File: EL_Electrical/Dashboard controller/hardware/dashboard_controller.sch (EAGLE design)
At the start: 48 parts, among them IC1 MCP2562-E_SN, IC2 MCP2515-I_SO, J1 22-05-7098-09, Q1 BSS138, Q2 BSS138, Q3 BSS138, Q6 BSS138

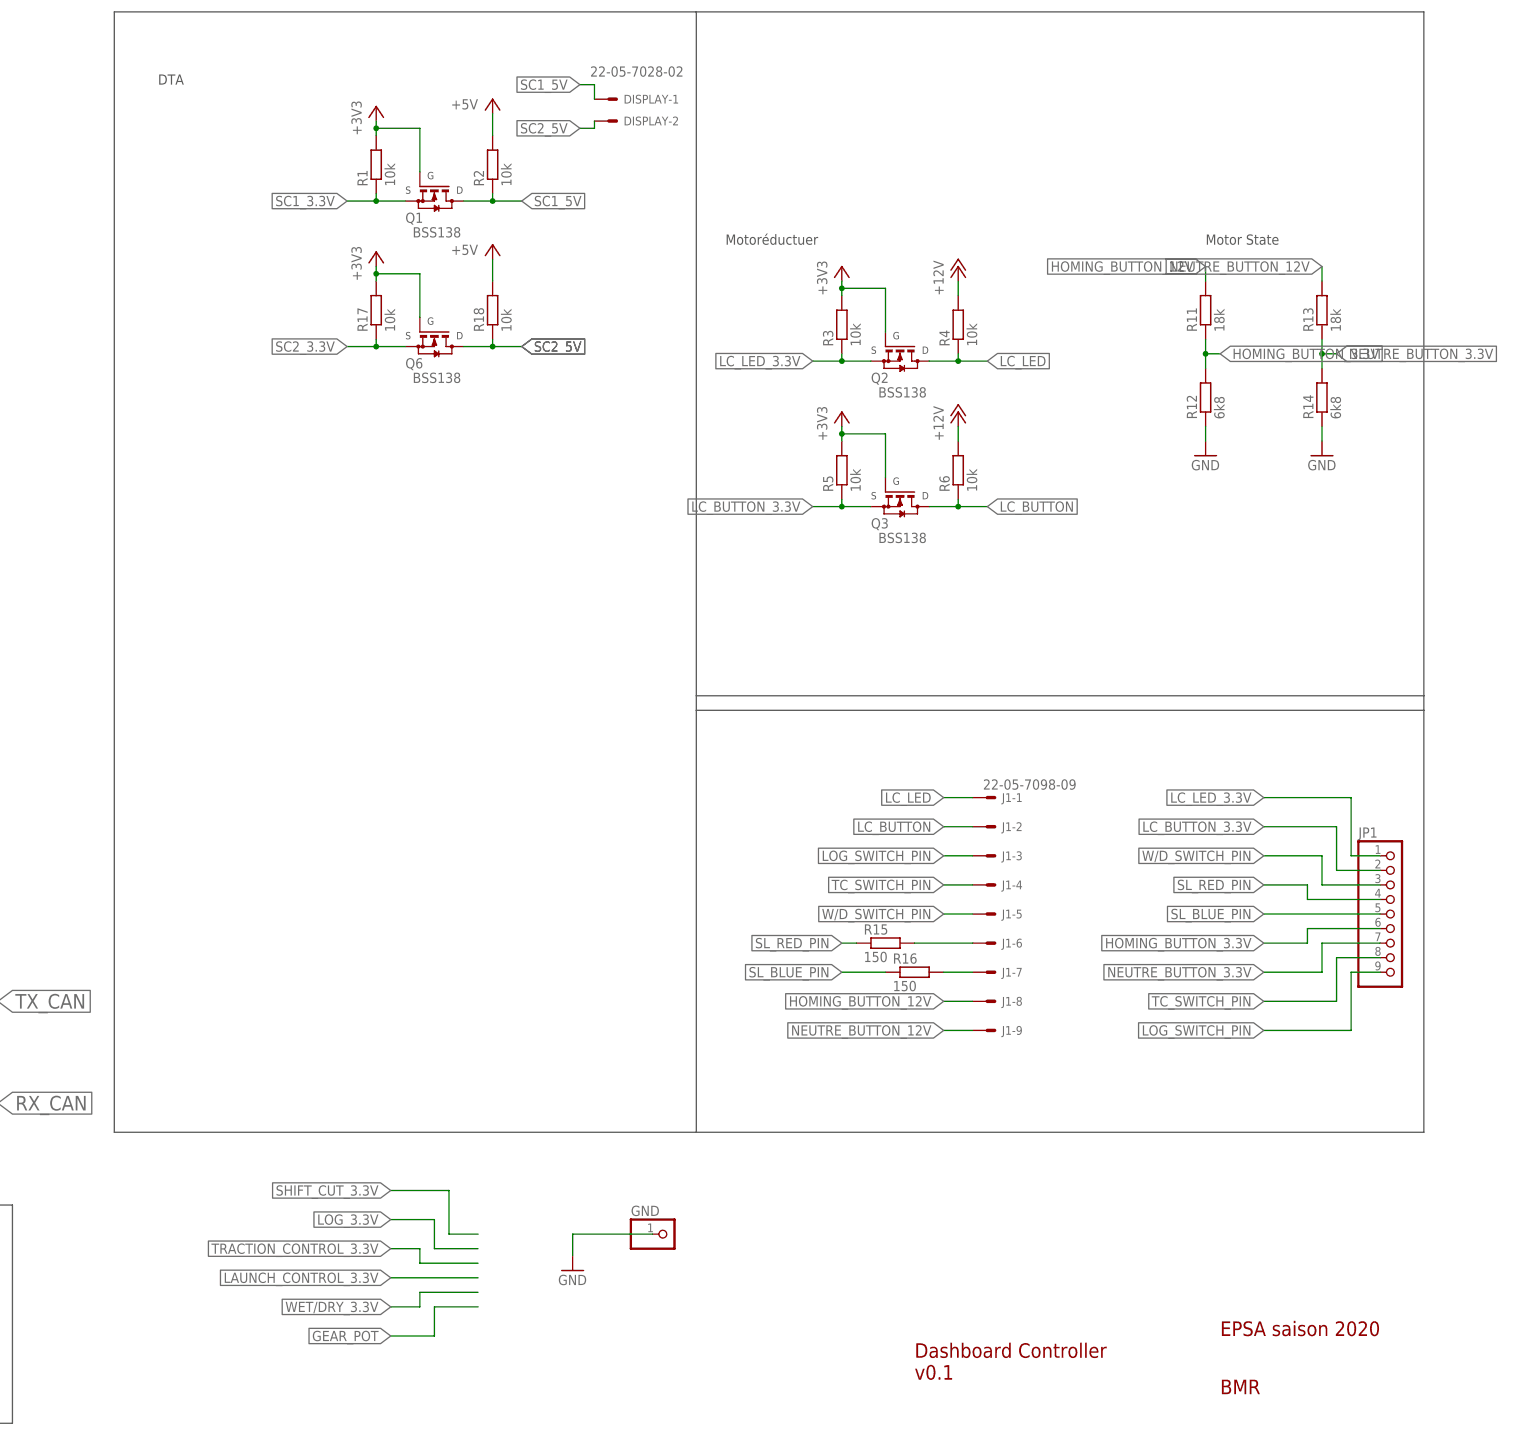
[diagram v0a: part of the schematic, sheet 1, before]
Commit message: Minor changes and missing connection fixed in Dashboard_controller
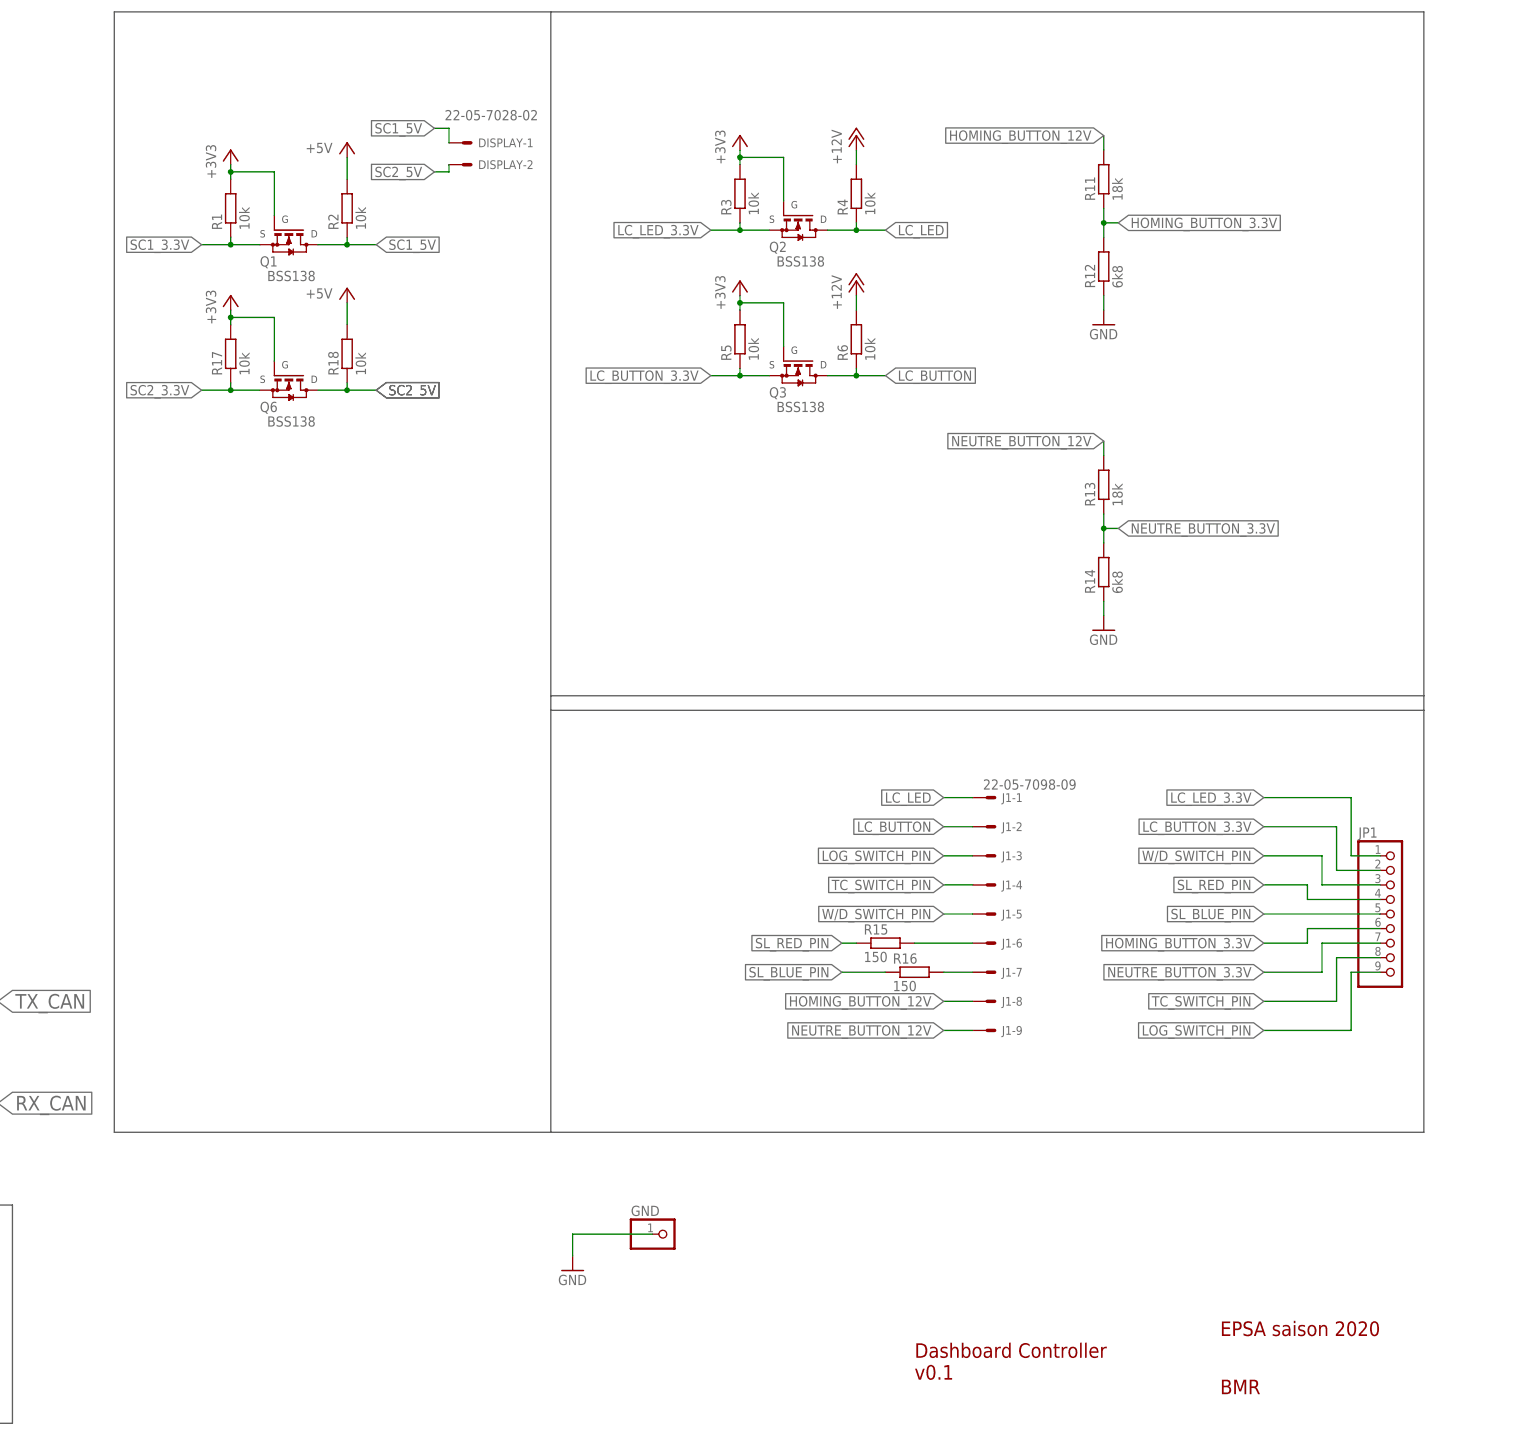
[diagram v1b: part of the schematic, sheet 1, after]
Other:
- note removed: "DTA"
- note removed: "Motor State"
- note removed: "Motoréductuer"
- moved on the sheet: DISPLAY-1, DISPLAY-2, Q1, Q2, Q3, Q6, R1, R11, R12, R13, R14, R17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

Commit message: Change circuit to drive the shift LEDs and Launch Control button
TODO: (re)change pin order to shorten 3.3V route (botton layer) and top layers route

TODO 2: add big capacitor
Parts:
- removed JP1: (no value), test_pin_DTA:PINHD-1X9
- removed Q3: BSS138, transistor-small-signal:BSS123
- added Q4, Q5: BSS138, transistor-small-signal:BSS123
- added R10, R7: 2k2, rcl:R-EU_R0805
- added R8: 10k, rcl:R-EU_R0805
- added R9: 330, rcl:R-EU_R0805
- added SL_5V: (no value), pinhead:PINHD-1X1
- added TEST_PINS: (no value), test_pin_DTA:PINHD-1X9
- R15: value 150 -> 10k
- R16: value 150 -> 330
- R5: value 10k -> 18k
- R6: value 10k -> 6k8
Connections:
- removed net LC_BUTTON: J1-2.S, Q3.D, R6.1
- removed net N$12: J1-6.S, R15.2
- removed net N$13: J1-7.S, R16.2
- new net LC_BUTTON_12V: J1-4.S, R5.2
- new net N$4: Q4.D, R7.1
- new net N$5: Q5.G, R15.2, R16.1
- new net N$8: Q4.G, R8.2, R9.1
- new net N$9: Q5.D, R10.1
- new net SL_BLUE: J1-2.S, R10.2
- new net SL_RED: J1-1.S, R7.2
- net +12V: no longer R6.2
- net +3V3: no longer Q3.G, R5.2
- net +5V: now also SL_5V.1
- net GND: now also Q4.S, Q5.S, R15.1, R6.1, R8.1
- net HOMING_BUTTON_3.3V: now also TEST_PINS.6; no longer JP1.6
- net LC_BUTTON_3.3V: now also R6.2, TEST_PINS.4; no longer JP1.2, Q3.S
- net LC_LED: now also J1-3.S; no longer J1-1.S
- net LC_LED_3.3V: now also TEST_PINS.3; no longer JP1.1
- net LOG_SWITCH_PIN: now also J1-5.S, TEST_PINS.9; no longer J1-3.S, JP1.9
- net NEUTRE_BUTTON_3.3V: now also TEST_PINS.7; no longer JP1.7
- net SL_BLUE_PIN: now also R16.2, TEST_PINS.2; no longer JP1.5, R16.1
- net SL_RED_PIN: now also R9.2, TEST_PINS.1; no longer JP1.4, R15.1
- net TC_SWITCH_PIN: now also J1-6.S, TEST_PINS.8; no longer J1-4.S, JP1.8
- net W/D_SWITCH_PIN: now also J1-7.S, TEST_PINS.5; no longer J1-5.S, JP1.3
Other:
- moved on the sheet: J1-1, J1-2, J1-3, J1-4, J1-5, J1-6, J1-7, J1-8, J1-9, R11, R12, R13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

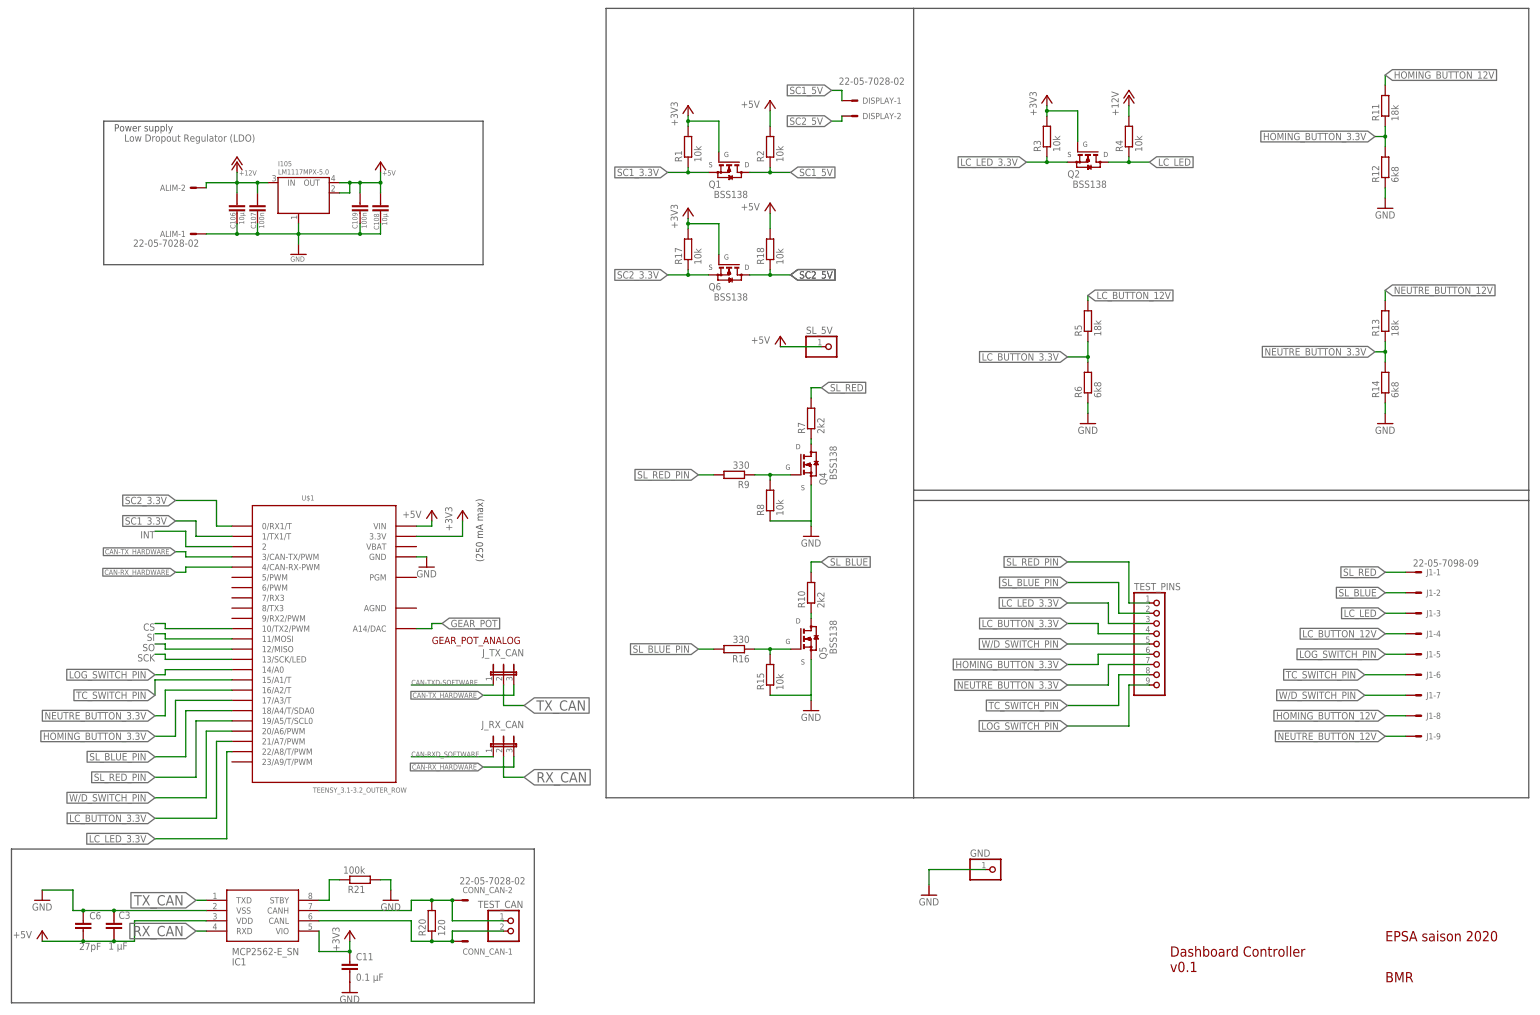
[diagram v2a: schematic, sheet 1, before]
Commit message: Delete LC_LED and change pin order and routes (Dashboard controller)
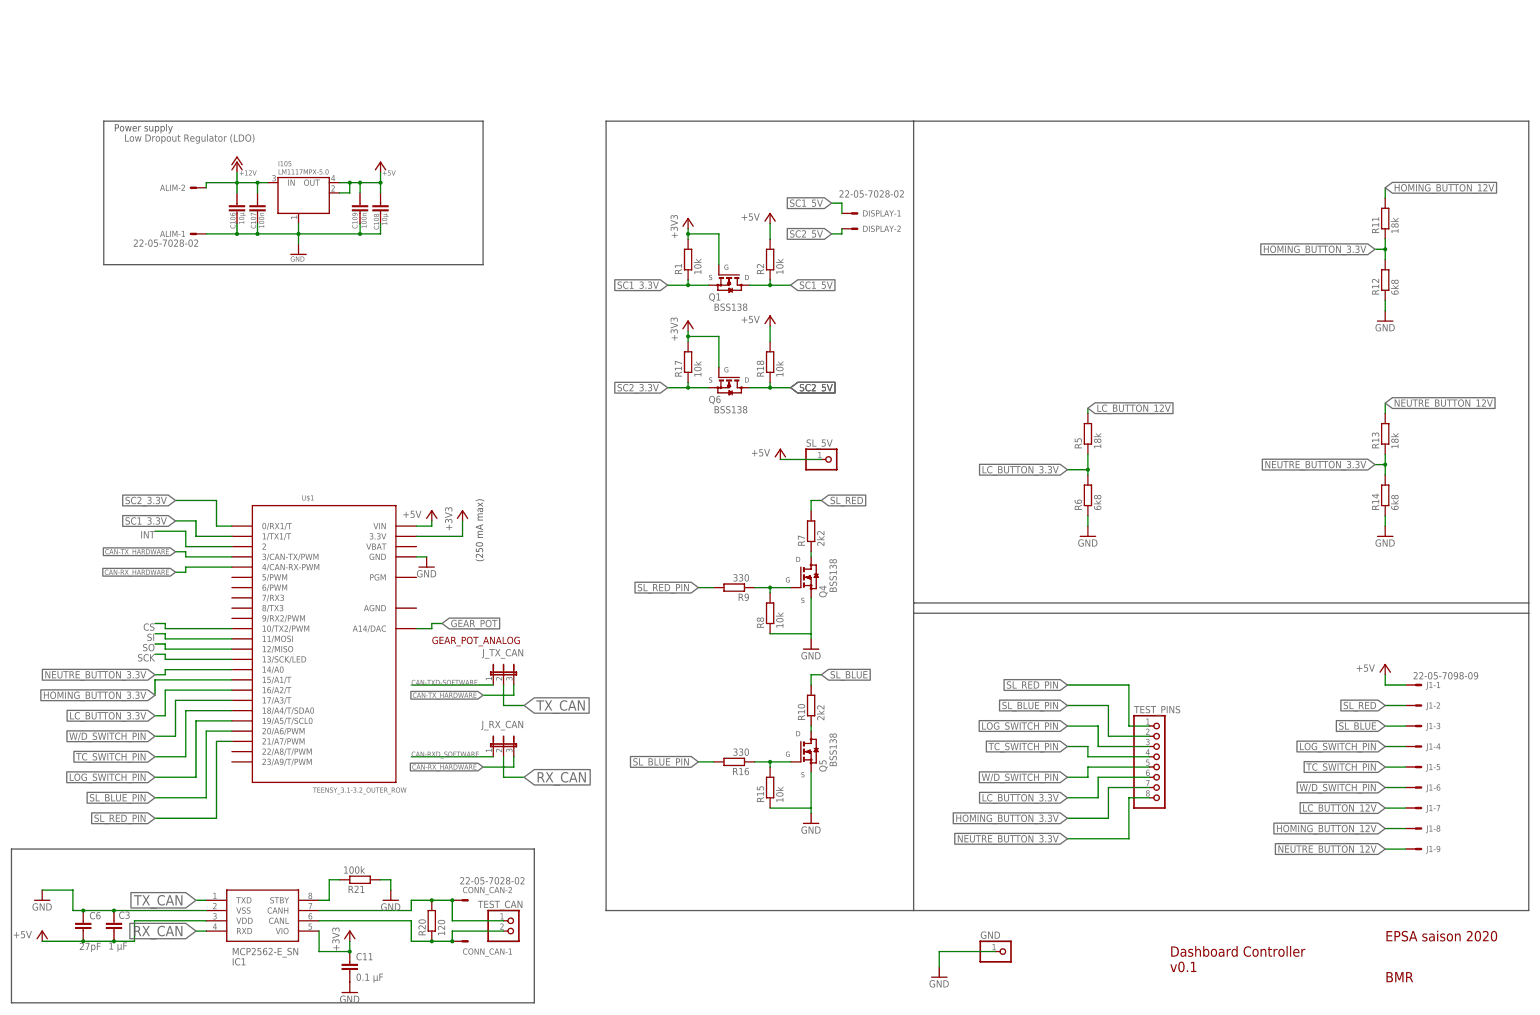
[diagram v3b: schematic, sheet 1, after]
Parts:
- removed Q2: BSS138, transistor-small-signal:BSS123
- removed R3, R4: 10k, rcl:R-EU_R0805
- TEST_PINS: device test_pin_DTA:PINHD-1X9 -> test_pin_DTA:PINHD-1X8
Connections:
- removed net LC_LED: J1-3.S, Q2.D, R4.1
- removed net LC_LED_3.3V: Q2.S, R3.1, TEST_PINS.3, U$1.22/A8/T/PWM
- net +12V: no longer R4.2
- net +3V3: no longer Q2.G, R3.2
- net +5V: now also J1-1.S
- net HOMING_BUTTON_3.3V: now also TEST_PINS.7, U$1.15/A1/T; no longer TEST_PINS.6, U$1.17/A3/T
- net LC_BUTTON_12V: now also J1-7.S; no longer J1-4.S
- net LC_BUTTON_3.3V: now also TEST_PINS.6, U$1.16/A2/T; no longer TEST_PINS.4, U$1.21/A7/PWM
- net LOG_SWITCH_PIN: now also J1-4.S, TEST_PINS.3, U$1.19/A5/T/SCL0; no longer J1-5.S, TEST_PINS.9, U$1.14/A0
- net NEUTRE_BUTTON_3.3V: now also TEST_PINS.8, U$1.14/A0; no longer TEST_PINS.7, U$1.16/A2/T
- net SL_BLUE: now also J1-3.S; no longer J1-2.S
- net SL_BLUE_PIN: now also U$1.20/A6/PWM; no longer U$1.18/A4/T/SDA0
- net SL_RED: now also J1-2.S; no longer J1-1.S
- net SL_RED_PIN: now also U$1.21/A7/PWM; no longer U$1.19/A5/T/SCL0
- net TC_SWITCH_PIN: now also J1-5.S, TEST_PINS.4, U$1.18/A4/T/SDA0; no longer J1-6.S, TEST_PINS.8, U$1.15/A1/T
- net W/D_SWITCH_PIN: now also J1-6.S, U$1.17/A3/T; no longer J1-7.S, U$1.20/A6/PWM
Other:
- moved on the sheet: DISPLAY-1, DISPLAY-2, GND, J1-1, J1-2, J1-3, J1-4, J1-5, J1-6, J1-7, J1-8, J1-9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
